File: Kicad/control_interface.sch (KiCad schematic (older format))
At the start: 4 parts

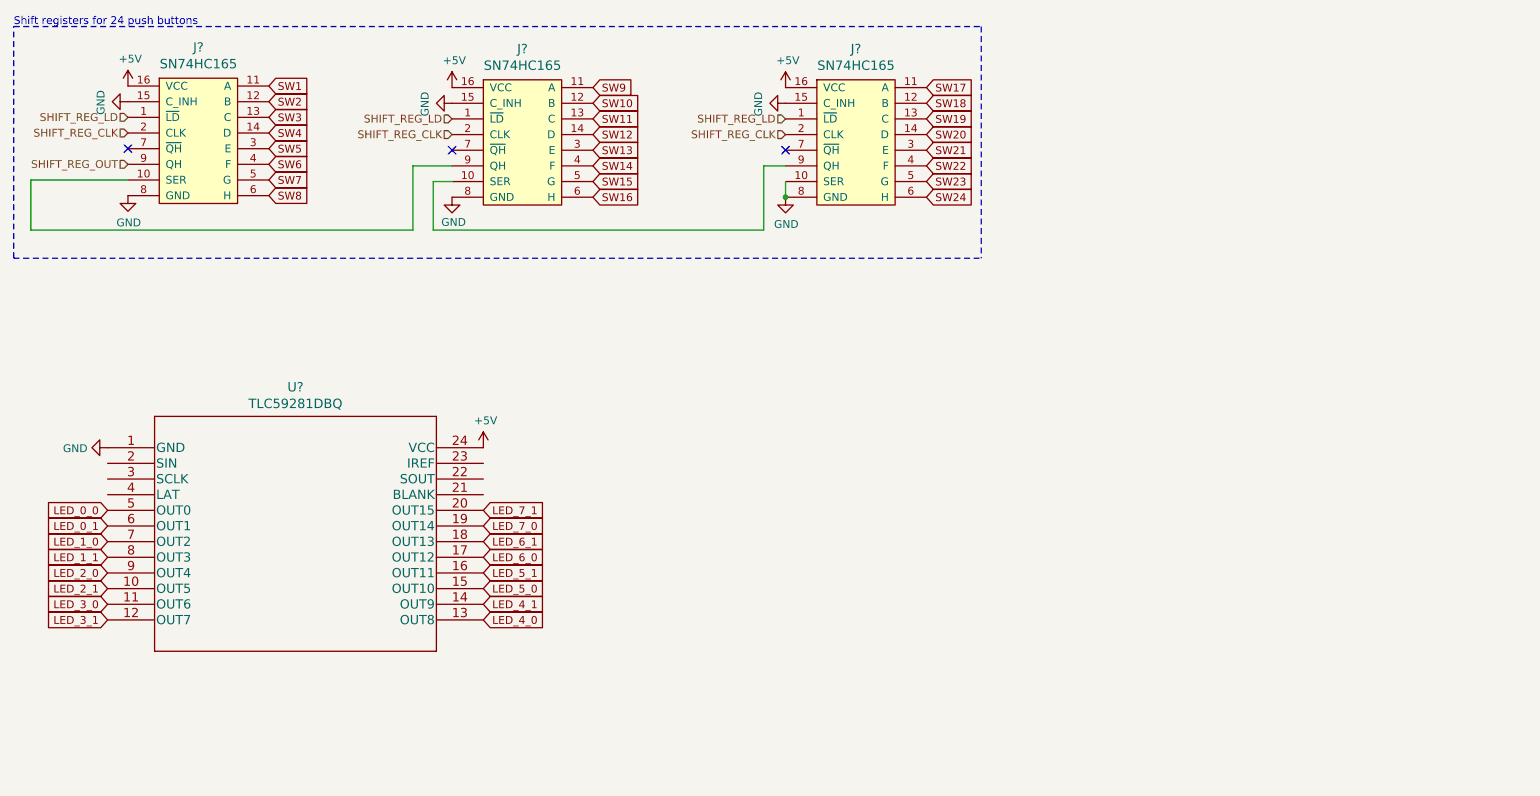
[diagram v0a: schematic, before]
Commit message: decoupling capacitors for stm32
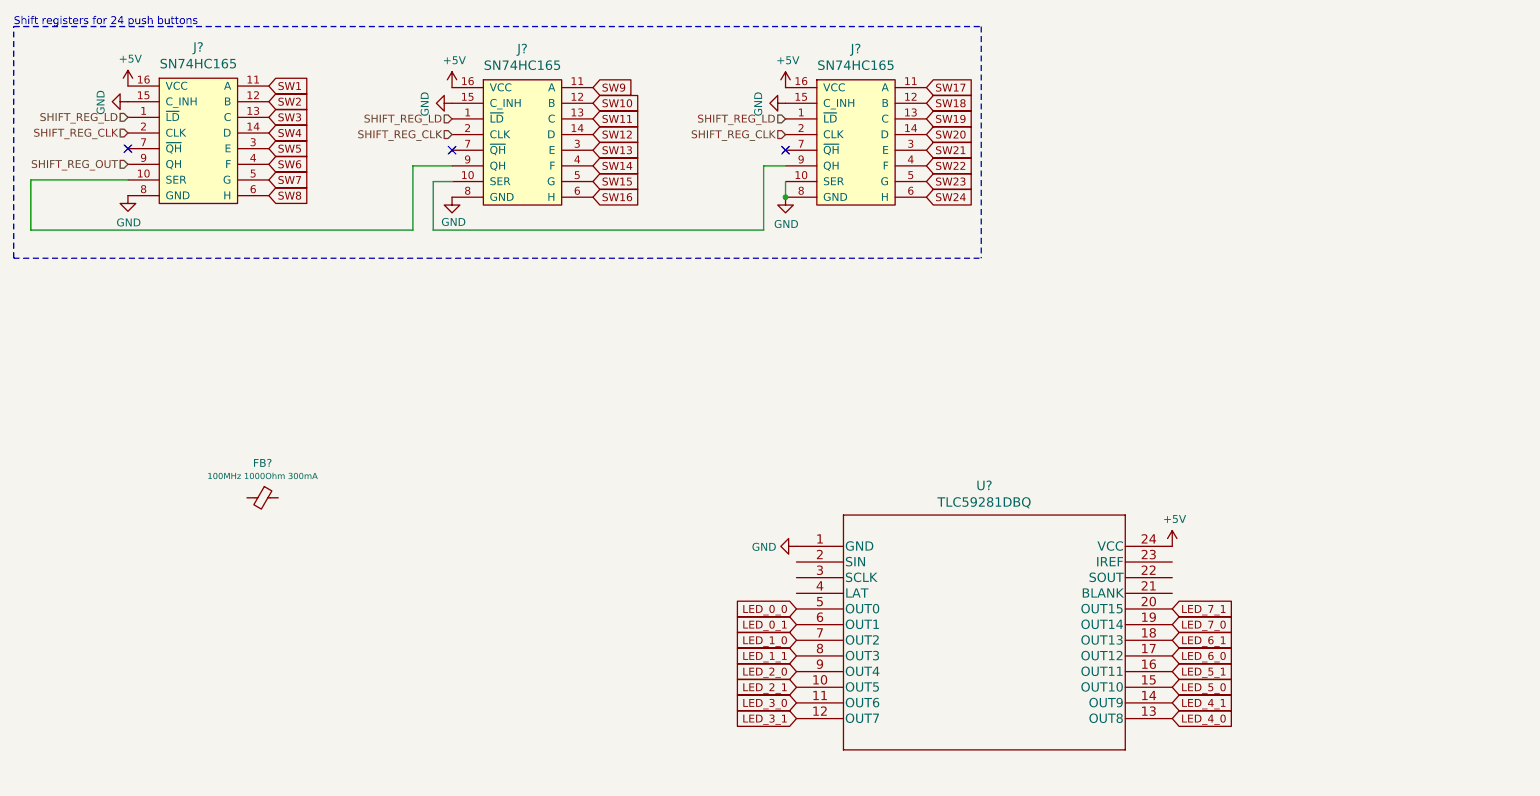
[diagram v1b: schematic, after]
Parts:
- added FB?: 100MHz 1000Ohm 300mA, symbol Device:Ferrite_Bead_Small
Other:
- moved on the sheet: U?
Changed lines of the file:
@@
 L eurorack_custom:ul_TLC59281DBQ_TLC59281DBQ U?
 U 1 1 5FE6AA44
-P 1430 3530
+P 5830 4160
 AR Path="/5FB96D72/5FE6AA44" Ref="U?"  Part="1"
 AR Path="/5FC5188F/5FE6AA44" Ref="U?"  Part="1"
 AR Path="/5FE50EBA/5FE6AA44" Ref="U?"  Part="1"
-F 0 "U?" H 2630 3917 60  0000 C CNN
-F 1 "TLC59281DBQ" H 2630 3811 60  0000 C CNN
-F 2 "Package_DFN_QFN:VQFN-24-1EP_4x4mm_P0.5mm_EP2.45x2.45mm" H 2630 3770 60  0001 C CNN
-F 3 "" H 1430 3530 60  0000 C CNN
-	1    1430 3530
-	1    0    0    -1
-$EndComp
-Text GLabel 1430 3930 0    50   Input ~ 0
+F 0 "U?" H 7030 4547 60  0000 C CNN
+F 1 "TLC59281DBQ" H 7030 4441 60  0000 C CNN
+F 2 "Package_DFN_QFN:VQFN-24-1EP_4x4mm_P0.5mm_EP2.45x2.45mm" H 7030 4400 60  0001 C CNN
+F 3 "" H 5830 4160 60  0000 C CNN
+	1    5830 4160
+	1    0    0    -1
+$EndComp
+Text GLabel 5830 4560 0    50   Input ~ 0
 LED_0_0
-Text GLabel 1430 4030 0    50   Input ~ 0
+Text GLabel 5830 4660 0    50   Input ~ 0
 LED_0_1
-Text GLabel 1430 4130 0    50   Input ~ 0
+Text GLabel 5830 4760 0    50   Input ~ 0
 LED_1_0
-Text GLabel 1430 4230 0    50   Input ~ 0
+Text GLabel 5830 4860 0    50   Input ~ 0
 LED_1_1
-Text GLabel 1430 4330 0    50   Input ~ 0
+Text GLabel 5830 4960 0    50   Input ~ 0
 LED_2_0
-Text GLabel 1430 4430 0    50   Input ~ 0
+Text GLabel 5830 5060 0    50   Input ~ 0
 LED_2_1
-Text GLabel 1430 4530 0    50   Input ~ 0
+Text GLabel 5830 5160 0    50   Input ~ 0
 LED_3_0
-Text GLabel 1430 4630 0    50   Input ~ 0
+Text GLabel 5830 5260 0    50   Input ~ 0
 LED_3_1
-Text GLabel 3830 3930 2    50   Input ~ 0
+Text GLabel 8230 4560 2    50   Input ~ 0
 LED_7_1
-Text GLabel 3830 4030 2    50   Input ~ 0
+Text GLabel 8230 4660 2    50   Input ~ 0
 LED_7_0
-Text GLabel 3830 4130 2    50   Input ~ 0
+Text GLabel 8230 4760 2    50   Input ~ 0
 LED_6_1
-Text GLabel 3830 4230 2    50   Input ~ 0
+Text GLabel 8230 4860 2    50   Input ~ 0
 LED_6_0
-Text GLabel 3830 4330 2    50   Input ~ 0
+Text GLabel 8230 4960 2    50   Input ~ 0
 LED_5_1
-Text GLabel 3830 4430 2    50   Input ~ 0
+Text GLabel 8230 5060 2    50   Input ~ 0
 LED_5_0
-Text GLabel 3830 4530 2    50   Input ~ 0
+Text GLabel 8230 5160 2    50   Input ~ 0
 LED_4_1
-Text GLabel 3830 4630 2    50   Input ~ 0
+Text GLabel 8230 5260 2    50   Input ~ 0
 LED_4_0
 $Comp
@@
 L power:+5V #PWR?
 U 1 1 5FE6AA92
-P 3830 3530
+P 8230 4160
 AR Path="/5FC5188F/5FE6AA92" Ref="#PWR?"  Part="1"
 AR Path="/5FE50EBA/5FE6AA92" Ref="#PWR?"  Part="1"
-F 0 "#PWR?" H 3830 3380 50  0001 C CNN
-F 1 "+5V" H 3845 3703 50  0000 C CNN
-F 2 "" H 3830 3530 50  0001 C CNN
-F 3 "" H 3830 3530 50  0001 C CNN
-	1    3830 3530
+F 0 "#PWR?" H 8230 4010 50  0001 C CNN
+F 1 "+5V" H 8245 4333 50  0000 C CNN
+F 2 "" H 8230 4160 50  0001 C CNN
+F 3 "" H 8230 4160 50  0001 C CNN
+	1    8230 4160
 	1    0    0    -1
 $EndComp
@@
 L power:GND #PWR?
 U 1 1 5FE6AA98
-P 1430 3530
+P 5830 4160
 AR Path="/5FC5188F/5FE6AA98" Ref="#PWR?"  Part="1"
 AR Path="/5FE50EBA/5FE6AA98" Ref="#PWR?"  Part="1"
-F 0 "#PWR?" H 1430 3280 50  0001 C CNN
-F 1 "GND" V 1435 3402 50  0000 R CNN
-F 2 "" H 1430 3530 50  0001 C CNN
-F 3 "" H 1430 3530 50  0001 C CNN
-	1    1430 3530
+F 0 "#PWR?" H 5830 3910 50  0001 C CNN
+F 1 "GND" V 5835 4032 50  0000 R CNN
+F 2 "" H 5830 4160 50  0001 C CNN
+F 3 "" H 5830 4160 50  0001 C CNN
+	1    5830 4160
 	0    1    1    0
 $EndComp
@@
 Wire Notes Line
 	830  2320 7010 2320
+$Comp
+L Device:Ferrite_Bead_Small FB?
+U 1 1 5FE8B2B8
+P 2420 3850
+F 0 "FB?" V 2199 3850 50  0000 C CNN
+F 1 "100MHz 1000Ohm 300mA" V 2282 3850 39  0000 C CNN
+F 2 "" V 2350 3850 50  0001 C CNN
+F 3 "~" H 2420 3850 50  0001 C CNN
+	1    2420 3850
+	0    1    1    0
+$EndComp
 $EndSCHEMATC

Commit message: adding SWD
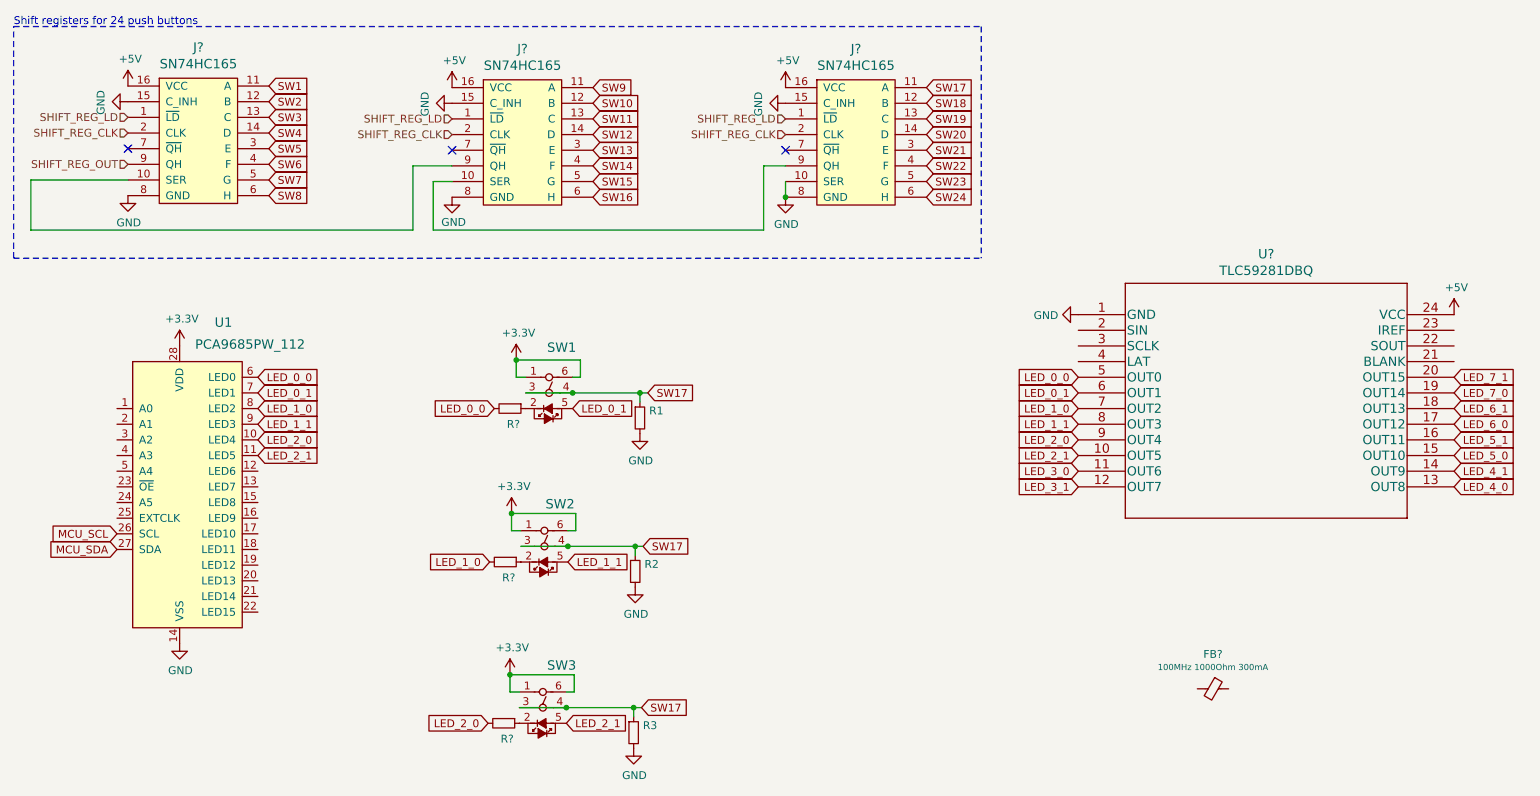
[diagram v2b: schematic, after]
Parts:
- added R1, R2, R3, R? (x3): R_Small, symbol Device:R_Small
- added SW1, SW2, SW3: Push, footprints:PB614_LED_SW_6pin, symbol sw_push_led_pb614:SW_Push_LED_PB614
- added U1: PCA9685PW_112, digikey-footprints:TSSOP-28_W4.40mm, symbol dk_PMIC-LED-Drivers:PCA9685PW_112
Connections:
- net GND: now also R1.2, R2.2, R3.2, U1.14 (VSS)
- net LED_0_0: now also R?.2, U1.6 (LED0)
- net LED_0_1: now also SW1.5, U1.7 (LED1)
- net LED_1_0: now also R?.2, U1.8 (LED2)
- net LED_1_1: now also SW2.5, U1.9 (LED3)
- net LED_2_0: now also R?.2, U1.10 (LED4)
- net LED_2_1: now also SW3.5, U1.11 (LED5)
- net SW17: now also R1.1, R2.1, R3.1, SW1.3, SW1.4, SW2.3, SW2.4, SW3.3, SW3.4
- new net: R?.1, SW1.2
- new net: R?.1, SW2.2
- new net: R?.1, SW3.2
- new net +3V3: SW1.1, SW1.6, SW2.1, SW2.6, SW3.1, SW3.6, U1.28 (VDD)
- new net MCU_SCL: U1.26 (SCL)
- new net MCU_SDA: U1.27 (SDA)
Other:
- moved on the sheet: FB?, U?
